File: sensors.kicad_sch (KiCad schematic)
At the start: 23 parts, among them U2 ACS724LLCTR-10AB-T, U3 UA9637A

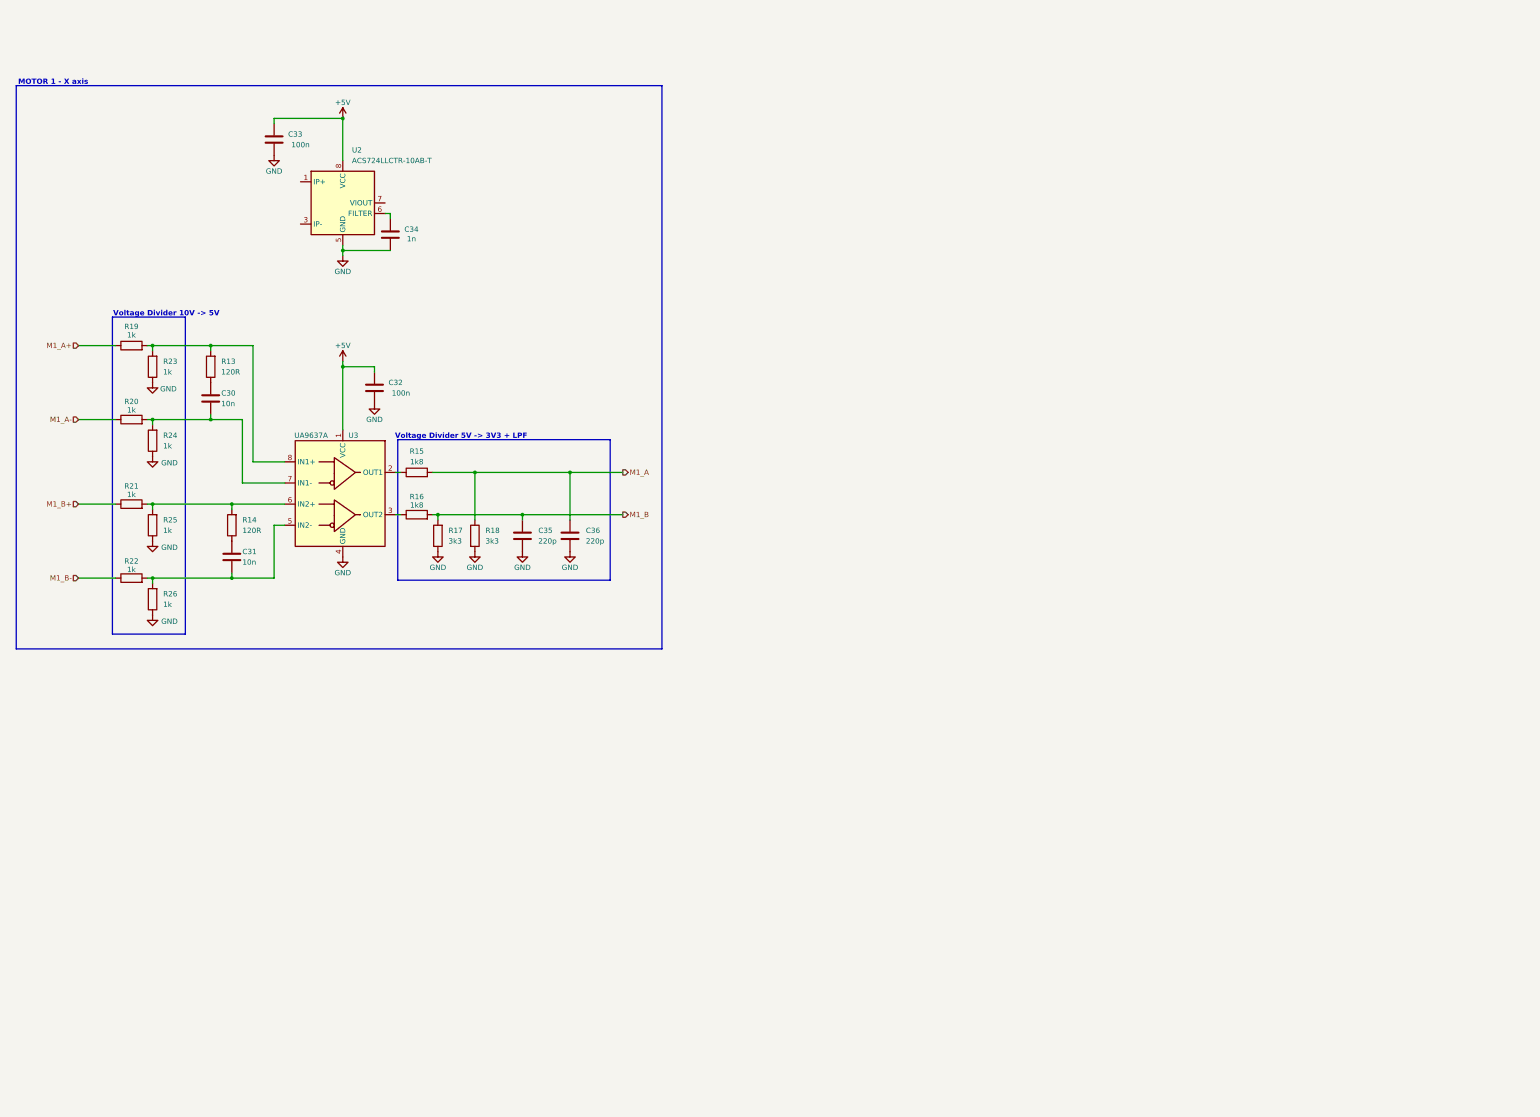
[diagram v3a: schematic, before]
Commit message: feat: linear encoders for all 3 dc motors
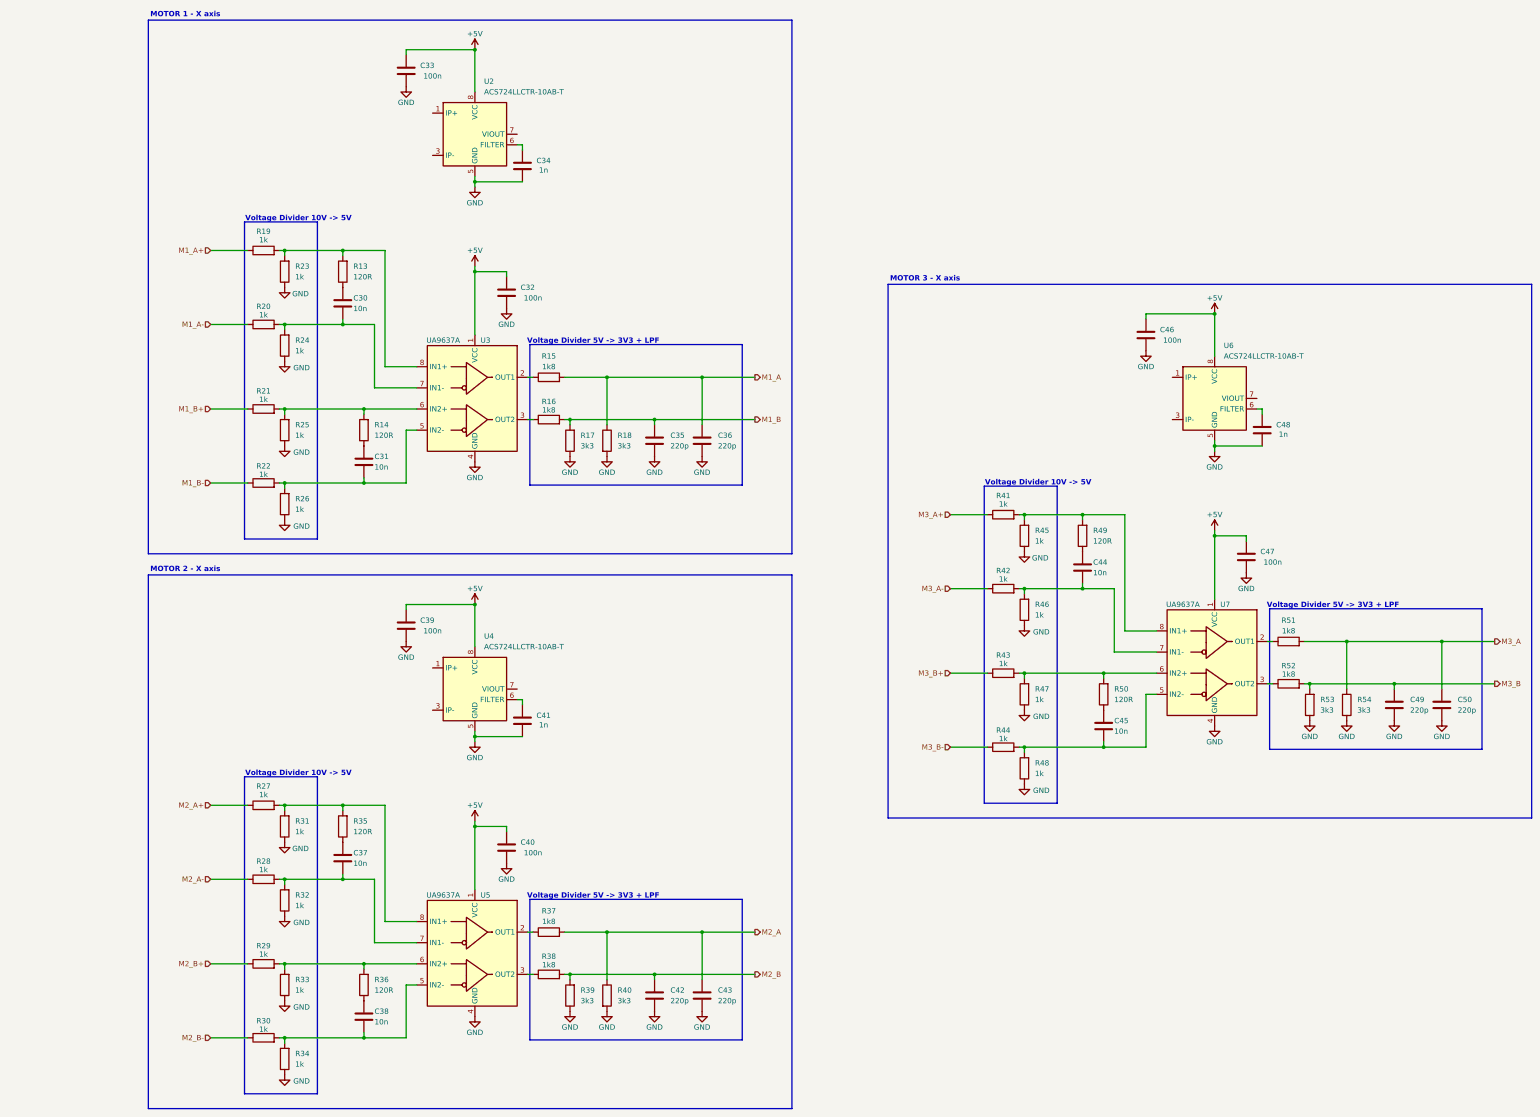
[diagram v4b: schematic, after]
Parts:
- added C37, C38, C44, C45: 10n, Capacitor_SMD:C_0603_1608Metric, symbol Device:C
- added C39, C40, C46, C47: 100n, Capacitor_SMD:C_0603_1608Metric, symbol Device:C
- added C41, C48: 1n, Capacitor_SMD:C_0603_1608Metric, symbol Device:C
- added C42, C43, C49, C50: 220p, symbol Device:C
- added R27, R28, R29, R30, R31, R32, R33, R34, R41, R42, R43, R44, R45, R46, R47, R48: 1k, symbol Device:R
- added R35, R36, R49, R50: 120R, Resistor_SMD:R_0603_1608Metric, symbol Device:R
- added R37, R38, R51, R52: 1k8, symbol Device:R
- added R39, R40, R53, R54: 3k3, symbol Device:R
- added U4, U6: ACS724LLCTR-10AB-T, Package_SO:SOIC-8_3.9x4.9mm_P1.27mm, symbol Sensor_Current:ACS724xLCTR-10AB
- added U5, U7: UA9637A, Package_SO:SOIC-8_3.9x4.9mm_P1.27mm, symbol Eagle_Main:UA9637A
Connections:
- net +5V: now also C39.1, C40.1, C46.1, C47.1, U4.8 (VCC), U5.1 (VCC), U6.8 (VCC), U7.1 (VCC)
- net GND: now also C39.2, C40.2, C41.2, C42.2, C43.2, C46.2, C47.2, C48.2, C49.2, C50.2, R31.1, R32.1, R33.1, R34.1, R39.1, R40.2, R45.1, R46.1, R47.1, R48.1, R53.1, R54.2, U4.5 (GND), U5.4 (GND), U6.5 (GND), U7.4 (GND)
- new net: R27.2, R31.2, R35.2, U5.8 (IN1+)
- new net: C37.2, R28.2, R32.2, U5.7 (IN1-)
- new net: R37.1, U5.2 (OUT1)
- new net: R38.1, U5.3 (OUT2)
- new net: C38.2, R30.2, R34.2, U5.5 (IN2-)
- new net: R29.2, R33.2, R36.2, U5.6 (IN2+)
- new net: C45.1, R50.1
- new net: C45.2, R44.2, R48.2, U7.5 (IN2-)
- new net: R51.1, U7.2 (OUT1)
- new net: C44.2, R42.2, R46.2, U7.7 (IN1-)
- new net: C44.1, R49.1
- new net: C38.1, R36.1
- new net: R52.1, U7.3 (OUT2)
- new net: R43.2, R47.2, R50.2, U7.6 (IN2+)
- new net: R41.2, R45.2, R49.2, U7.8 (IN1+)
- new net: C37.1, R35.1
- new net: C48.1, U6.6 (FILTER)
- new net: C41.1, U4.6 (FILTER)
- new net: U6.1 (IP+), U6.2 (IP+)
- new net: U6.3 (IP-), U6.4 (IP-)
- new net: U4.1 (IP+), U4.2 (IP+)
- new net: U4.3 (IP-), U4.4 (IP-)
- new net M2_A: C43.1, R37.2, R40.1
- new net M2_A+: R27.1
- new net M2_A-: R28.1
- new net M2_B: C42.1, R38.2, R39.2
- new net M2_B+: R29.1
- new net M2_B-: R30.1
- new net M3_A: C50.1, R51.2, R54.1
- new net M3_A+: R41.1
- new net M3_A-: R42.1
- new net M3_B: C49.1, R52.2, R53.2
- new net M3_B+: R43.1
- new net M3_B-: R44.1
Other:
- note added: "MOTOR 2 - X axis"
- note added: "MOTOR 3 - X axis"
- moved on the sheet: C30, C31, C32, C33, C34, C35, C36, R13, R14, R15, R16, R17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

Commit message: fix: no voltage divider is needed on encoders input
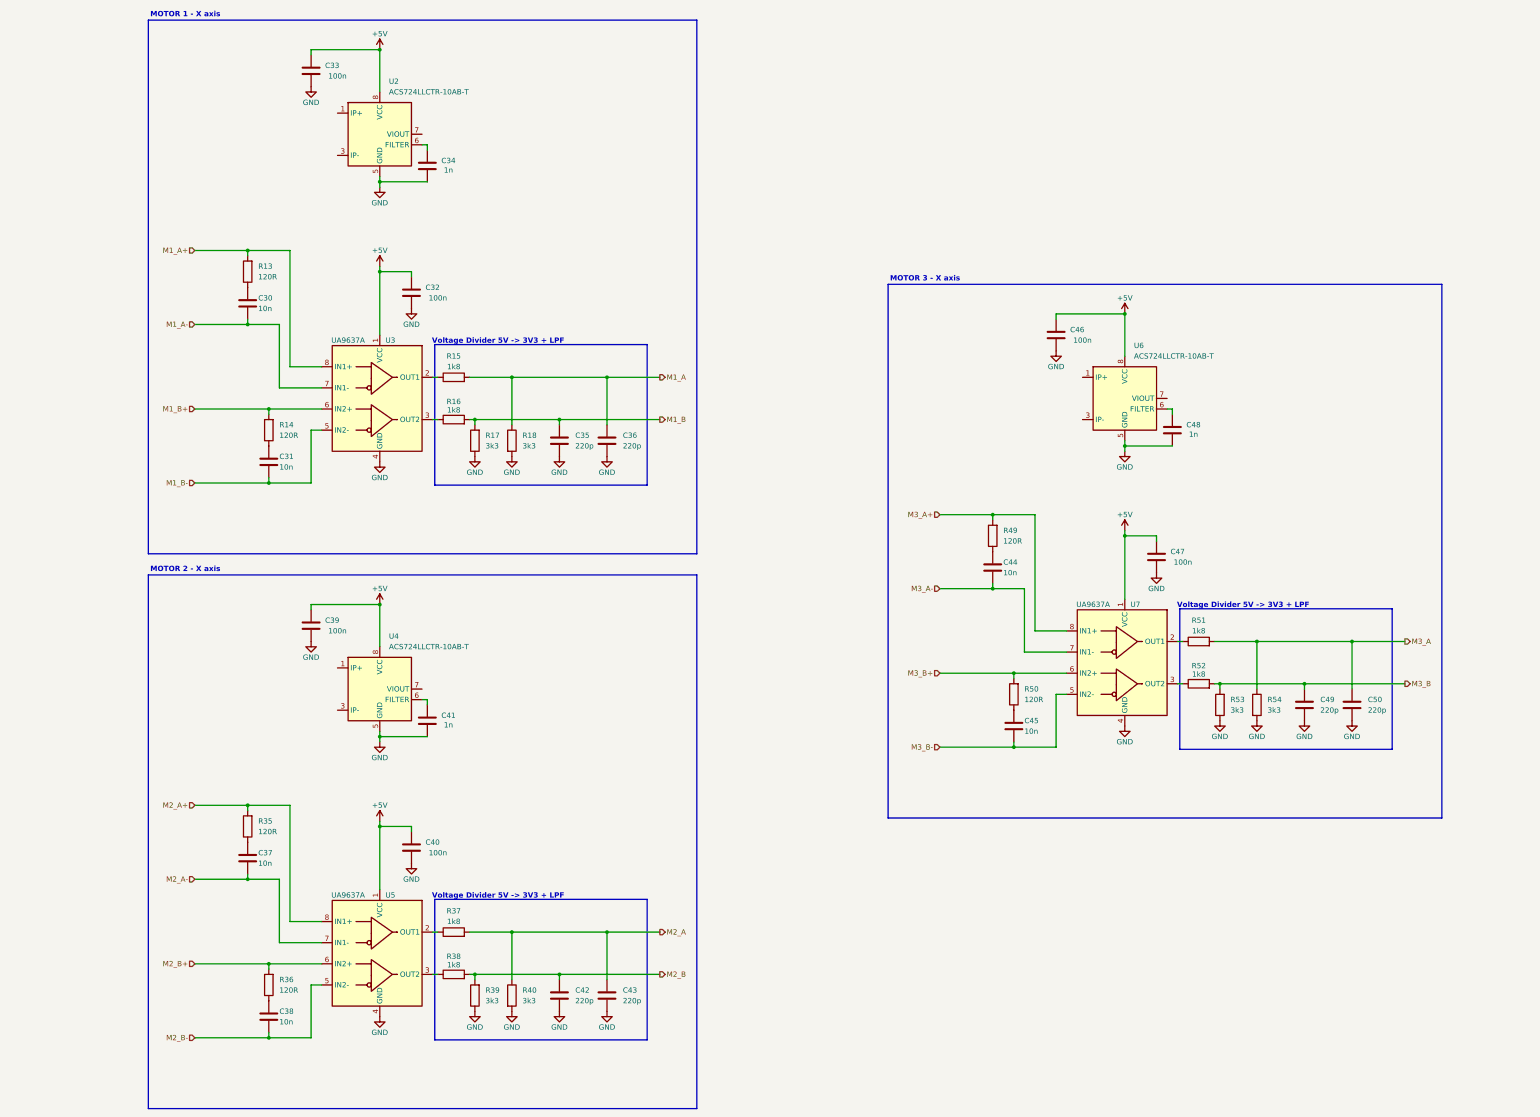
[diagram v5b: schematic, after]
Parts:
- removed R19, R20, R21, R22, R23, R24, R25, R26, R27, R28, R29, R30, R31, R32, R33, R34, R41, R42, R43, R44, R45, R46, R47, R48: 1k, symbol Device:R
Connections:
- net M1_A+: now also R13.2, U3.8 (IN1+)
- net M1_A-: now also C30.2, U3.7 (IN1-)
- net M1_B+: now also R14.2, U3.6 (IN2+)
- net M1_B-: now also C31.2, U3.5 (IN2-)
- net M2_A+: now also R35.2, U5.8 (IN1+)
- net M2_A-: now also C37.2, U5.7 (IN1-)
- net M2_B+: now also R36.2, U5.6 (IN2+)
- net M2_B-: now also C38.2, U5.5 (IN2-)
- net M3_A+: now also R49.2, U7.8 (IN1+)
- net M3_A-: now also C44.2, U7.7 (IN1-)
- net M3_B+: now also R50.2, U7.6 (IN2+)
- net M3_B-: now also C45.2, U7.5 (IN2-)
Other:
- note removed: "Voltage Divider 10V -> 5V"
- moved on the sheet: C30, C31, C32, C33, C34, C35, C36, C37, C38, C39, C40, C41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

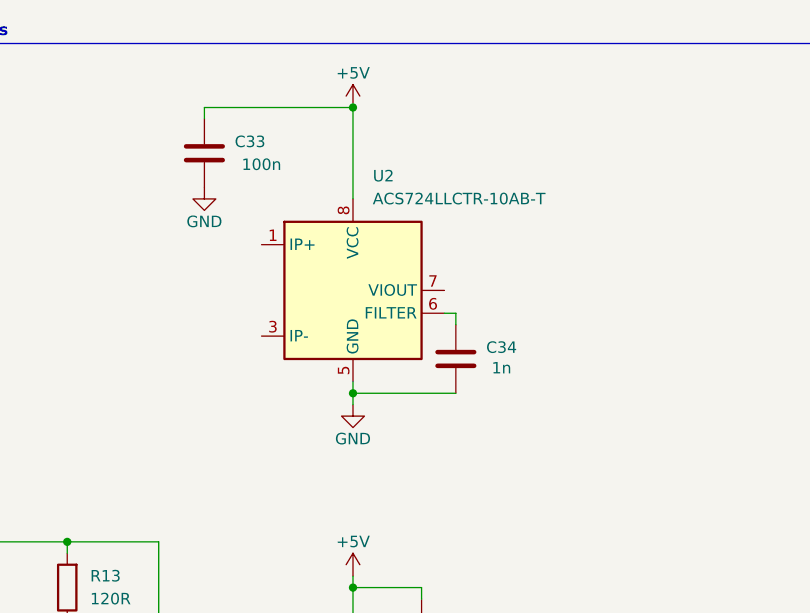
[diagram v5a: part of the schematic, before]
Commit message: fix: missing footprints and new current sensor
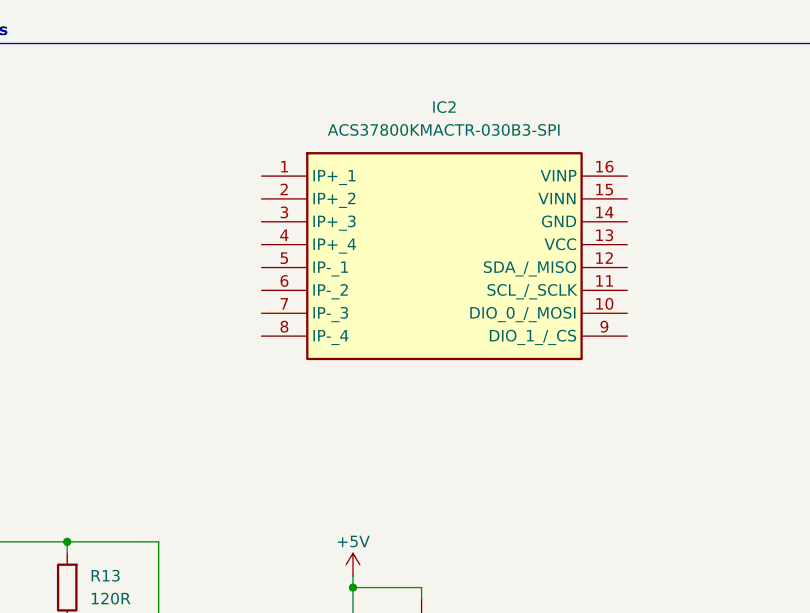
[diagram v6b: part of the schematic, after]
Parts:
- removed C33: 100n, Capacitor_SMD:C_0603_1608Metric, symbol Device:C
- removed C34: 1n, Capacitor_SMD:C_0603_1608Metric, symbol Device:C
- removed U2: ACS724LLCTR-10AB-T, Package_SO:SOIC-8_3.9x4.9mm_P1.27mm, symbol Sensor_Current:ACS724xLCTR-10AB
- added IC2: ACS37800KMACTR-030B3-SPI, Local:SOIC127P1030X265-16N, symbol ACS:ACS37800KMACTR-030B3-SPI
- C35, C36, C42, C43, C49, C50: footprint (none) -> Capacitor_SMD:C_0603_1608Metric
- R15, R16, R17, R18, R37, R38, R39, R40, R51, R52, R53, R54: footprint (none) -> Resistor_SMD:R_0603_1608Metric

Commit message: fix: minors
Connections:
- net DC_1_IN: now reaches IC2.1 (IP+_1)
- net DC_1_IN: now also IC2.2 (IP+_2), IC2.3 (IP+_3), IC2.4 (IP+_4)
- net DC_1_OUT: now reaches IC2.5 (IP-_1)
- net DC_1_OUT: now also IC2.6 (IP-_2), IC2.7 (IP-_3), IC2.8 (IP-_4)
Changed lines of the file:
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@@
+	)
+	(junction
+		(at 91.44 46.99)
+		(diameter 0)
+		(color 0 0 0 0)
 	)
 	(junction
@@
 	)
 	(junction
+		(at 91.44 38.1)
+		(diameter 0)
+		(color 0 0 0 0)
+	)
+	(junction
+		(at 91.44 48.26)
+		(diameter 0)
+		(color 0 0 0 0)
+	)
+	(junction
 		(at 101.6 78.74)
 		(diameter 0)
@@
 	)
 	(junction
+		(at 91.44 36.83)
+		(diameter 0)
+		(color 0 0 0 0)
+	)
+	(junction
+		(at 91.44 35.56)
+		(diameter 0)
+		(color 0 0 0 0)
+	)
+	(junction
 		(at 133.35 237.49)
 		(diameter 0)
@@
 		(color 0 0 0 0)
 	)
+	(junction
+		(at 91.44 45.72)
+		(diameter 0)
+		(color 0 0 0 0)
+	)
 	(polyline
 		(pts
@@
 		)
 	)
+	(wire
+		(pts
+			(xy 78.74 46.99) (xy 91.44 46.99)
+		)
+		(stroke
+			(width 0)
+			(type default)
+		)
+	)
 	(polyline
 		(pts
@@
 	(wire
 		(pts
+			(xy 78.74 36.83) (xy 91.44 36.83)
+		)
+		(stroke
+			(width 0)
+			(type default)
+		)
+	)
+	(wire
+		(pts
 			(xy 266.7 165.1) (xy 259.08 165.1)
 		)
@@
 		)
 	)
+	(wire
+		(pts
+			(xy 91.44 48.26) (xy 91.44 50.8)
+		)
+		(stroke
+			(width 0)
+			(type default)
+		)
+	)
 	(polyline
 		(pts
@@
 	(wire
 		(pts
+			(xy 91.44 38.1) (xy 91.44 40.64)
+		)
+		(stroke
+			(width 0)
+			(type default)
+		)
+	)
+	(wire
+		(pts
 			(xy 156.21 104.14) (xy 156.21 115.57)
 		)
@@
 	(wire
 		(pts
+			(xy 91.44 36.83) (xy 91.44 38.1)
+		)
+		(stroke
+			(width 0)
+			(type default)
+		)
+	)
+	(wire
+		(pts
 			(xy 57.15 245.11) (xy 74.93 245.11)
 		)
@@
 	(wire
 		(pts
+			(xy 91.44 33.02) (xy 91.44 35.56)
+		)
+		(stroke
+			(width 0)
+			(type default)
+		)
+	)
+	(wire
+		(pts
 			(xy 264.16 90.17) (xy 264.16 88.9)
 		)
@@
 		)
 	)
+	(wire
+		(pts
+			(xy 91.44 46.99) (xy 91.44 48.26)
+		)
+		(stroke
+			(width 0)
+			(type default)
+		)
+	)
 	(polyline
 		(pts
@@
 	(wire
 		(pts
+			(xy 91.44 46.99) (xy 91.44 45.72)
+		)
+		(stroke
+			(width 0)
+			(type default)
+		)
+	)
+	(wire
+		(pts
 			(xy 124.46 114.3) (xy 144.78 114.3)
 		)
@@
 	(wire
 		(pts
+			(xy 91.44 45.72) (xy 91.44 43.18)
+		)
+		(stroke
+			(width 0)
+			(type default)
+		)
+	)
+	(wire
+		(pts
 			(xy 101.6 210.82) (xy 101.6 212.09)
 		)
@@
 		(pts
 			(xy 256.54 170.18) (xy 256.54 154.94)
+		)
+		(stroke
+			(width 0)
+			(type default)
+		)
+	)
+	(wire
+		(pts
+			(xy 91.44 35.56) (xy 91.44 36.83)
 		)
 		(stroke
@@
 	(text "Voltage Divider 5V -> 3V3 + LPF"
 		(exclude_from_sim no)
-		(at 130.048 95.504 0)
+		(at 131.064 95.504 0)
 		(effects
 			(font
@@
 				(bold yes)
 			)
+		)
+	)
+	(hierarchical_label "DC_1_OUT"
+		(shape output)
+		(at 78.74 46.99 180)
+		(effects
+			(font
+				(size 1.27 1.27)
+			)
+			(justify right)
 		)
 	)
@@
 		(effects
 			(font
+				(size 1.27 1.27)
+			)
+			(justify right)
+		)
+	)
+	(hierarchical_label "DC_1_IN"
+		(shape input)
+		(at 78.74 36.83 180)
+		(effects
+			(font

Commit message: feat: current sensor setup
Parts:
- removed C41, C48: 1n, Capacitor_SMD:C_0603_1608Metric, symbol Device:C
- removed C46: 100n, Capacitor_SMD:C_0603_1608Metric, symbol Device:C
- removed U4, U6: ACS724LLCTR-10AB-T, Package_SO:SOIC-8_3.9x4.9mm_P1.27mm, symbol Sensor_Current:ACS724xLCTR-10AB
- added C33, C34: 100n, Capacitor_SMD:C_0603_1608Metric, symbol Device:C
- added IC3, IC4: ACS37800KMACTR-030B3-SPI, Local:SOIC127P1030X265-16N, symbol ACS:ACS37800KMACTR-030B3-SPI
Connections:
- net +5V: no longer C39.1
- net GND: now also IC2.14 (GND), IC2.15 (VINN), IC2.16 (VINP), C33.2, C34.2, IC3.14 (GND), IC3.15 (VINN), IC3.16 (VINP), IC4.14 (GND), IC4.15 (VINN), IC4.16 (VINP)
- net SPI4_MOSI: now reaches IC2.10 (DIO_0_/_MOSI)
- net SPI4_MOSI: now also IC3.10 (DIO_0_/_MOSI), IC4.10 (DIO_0_/_MOSI)
- net SPI4_SCK: now reaches IC2.11 (SCL_/_SCLK)
- net SPI4_SCK: now also IC3.11 (SCL_/_SCLK), IC4.11 (SCL_/_SCLK)
- net SPI4_MISO: now reaches IC2.12 (SDA_/_MISO)
- net SPI4_MISO: now also IC3.12 (SDA_/_MISO), IC4.12 (SDA_/_MISO)
- net +3V3: now reaches IC2.13 (VCC)
- net +3V3: now also C39.1, C33.1, C34.1, IC3.13 (VCC), IC4.13 (VCC)
- net SPI4_CSS_X: now reaches IC2.9 (DIO_1_/_CS)
- new net DC_2_IN: IC3.1 (IP+_1), IC3.2 (IP+_2), IC3.3 (IP+_3), IC3.4 (IP+_4)
- new net DC_2_OUT: IC3.5 (IP-_1), IC3.6 (IP-_2), IC3.7 (IP-_3), IC3.8 (IP-_4)
- new net DC_3_IN: IC4.1 (IP+_1), IC4.2 (IP+_2), IC4.3 (IP+_3), IC4.4 (IP+_4)
- new net DC_3_OUT: IC4.5 (IP-_1), IC4.6 (IP-_2), IC4.7 (IP-_3), IC4.8 (IP-_4)
- new net SPI4_CSS_Y1: IC3.9 (DIO_1_/_CS)
- new net SPI4_CSS_Y2: IC4.9 (DIO_1_/_CS)
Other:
- note added: "MOTOR 2 - Y1 axis"
- note added: "MOTOR 3 - Y2 axis"
- note removed: "MOTOR 2 - X axis"
- note removed: "MOTOR 3 - X axis"
